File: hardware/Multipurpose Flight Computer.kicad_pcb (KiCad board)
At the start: 2 copper layers, 34.9 x 44.6 mm, 79 parts, among them J1 Screw_Terminal_01x02, J2 Conn_01x03, J3 Conn_01x03, SW1 TS-1088-AR02016, SW2 TS-1088-AR02016, U1 BQ25883RGER, U2 ICM-45686, U3 STM32F722RETx, U4 BMP580, U5 TPS63070RNMR, U6 LMR51430, X1 X322525MOB4SI, X2 Q13FC1350000400

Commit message: Updating KiCad
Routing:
- net GND: track 93.6 -> 98.2 mm
- net /BTST: vias 3 -> 2
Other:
- board size 34.9 x 44.6 mm -> 35.4 x 44.6 mm
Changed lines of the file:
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@@
 		(tags "resistor")
 		(property "Reference" "R15"
-			(at 2.59 0.15 0)
+			(at 0.015178 2.9 0)
 			(layer "F.SilkS")
 			(effects
@@
 		(tags "resistor")
 		(property "Reference" "R14"
-			(at -2.56 -0.05 0)
+			(at 0.064822 -2.6 0)
 			(layer "F.SilkS")
 			(effects
@@
 	)
 	(gr_rect
-		(start 125 120.4)
-		(end 159.95 165)
+		(start 124.95 120.75)
+		(end 160.35 165.35)
 		(stroke
 			(width 0.2)
@@
 	)
 	(segment
+		(start 148.965 159.7)
+		(end 148.965 160.575)
+		(width 0.3)
+		(layer "F.Cu")
+		(net 1)
+	)
+	(segment
 		(start 144.620927 147.55)
 		(end 144.125 147.55)
@@
 	)
 	(segment
+		(start 148.97 160.62)
+		(end 148.99 160.6)
+		(width 0.3)
+		(layer "F.Cu")
+		(net 1)
+	)
+	(segment
 		(start 151.300001 147.4)
 		(end 154.21 144.490001)
@@
 	)
 	(segment
+		(start 148.99 158.9)
+		(end 148.99 159.675)
+		(width 0.3)
+		(layer "F.Cu")
+		(net 1)
+	)
+	(segment
 		(start 148.174822 156.65)
 		(end 147.45 156.65)
@@
 	)
 	(segment
+		(start 148.97 161.45)
+		(end 148.97 160.62)
+		(width 0.3)
+		(layer "F.Cu")
+		(net 1)
+	)
+	(segment
 		(start 137.55 135.498)
 		(end 137.051 134.999)
@@
 	)
 	(segment
+		(start 148.965 158.875)
+		(end 148.99 158.9)
+		(width 0.3)
+		(layer "F.Cu")
+		(net 1)
+	)
+	(segment
 		(start 148.83 133.05)
 		(end 150.15 133.05)
@@
 	)
 	(segment
+		(start 148.99 159.675)
+		(end 148.965 159.7)
+		(width 0.3)
+		(layer "F.Cu")
+		(net 1)
+	)
+	(segment
 		(start 151.95 158.05)
 		(end 151.95 158.55)
@@
 	)
 	(segment
+		(start 148.965 158.05)
+		(end 148.965 158.875)
+		(width 0.3)
+		(layer "F.Cu")
+		(net 1)
+	)
+	(segment
 		(start 149.274822 156.65)
 		(end 148.174822 156.65)
@@
 	)
 	(segment
+		(start 148.97 162.27)
+		(end 149.2 162.5)
+		(width 0.3)
+		(layer "F.Cu")
+		(net 1)
+	)
+	(segment
 		(start 138.049 134.999)
 		(end 141.949 134.999)
@@
 	)
 	(segment
+		(start 148.965 160.575)
+		(end 148.99 160.6)
+		(width 0.3)
+		(layer "F.Cu")
+		(net 1)
+	)
+	(segment
 		(start 128.010124 149.66802)
 		(end 127.4382 150.239944)
@@
 	)
 	(segment
+		(start 148.97 161.45)
+		(end 148.97 162.27)
+		(width 0.3)
+		(layer "F.Cu")
+		(net 1)
+	)
+	(segment
 		(start 154.399822 158.6)
 		(end 156.070822 160.271)
@@
 	)
 	(via
-		(at 150.100001 147.05)
-		(size 0.6)
-		(drill 0.3)
-		(layers "F.Cu" "B.Cu")
-		(net 6)
-	)
-	(via
 		(at 149.950001 151.45)
 		(size 0.6)
@@
 		(layers "F.Cu" "B.Cu")
 		(hatch edge 0.5)
-		(connect_pads
+		(connect_pads yes
 			(clearance 0.5)
 		)
@@
 		(polygon
 			(pts
-				(xy 125.9 121.1) (xy 159.15 121.2) (xy 159.45 164.05) (xy 125.75 164.2)
+				(xy 121.95 117.9) (xy 166.05 117.15) (xy 167.15 168.4) (xy 121.25 167.35)
 			)
 		)

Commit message: Finishing Touches
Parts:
- added H1: MountingHole, MountingHole:MountingHole_2.2mm_M2_DIN965_Pad_TopBottom, F.Cu at (156.7, 124.8)
- moved C28 31.2 mm to (130.1, 137.5), turned to 90 degrees
- moved C19 29.1 mm to (128.3, 138.2), turned to 180 degrees
- moved C20 25.7 mm to (127.3, 139.9)
- moved C24 23.1 mm to (133.8, 140.4), turned to 45 degrees
- moved C23 22.1 mm to (137.4, 140.7), turned to -45 degrees
- moved C30 18.4 mm to (133.3, 156.0), turned to 45 degrees
- moved C26 17.7 mm to (131.8, 156.1), turned to -135 degrees
- moved C25 11.6 mm to (141.3, 151.7), turned to -90 degrees
- moved C31 11.0 mm to (142.2, 152.0), turned to -90 degrees
- moved R7 1.25 mm to (142.4, 148.6)
- moved R11 0.53 mm to (143.8, 151.8)
- moved C29 0.38 mm to (135.5, 139.8), turned to 0 degrees
- moved R10 0.34 mm to (143.7, 150.9)
- moved R9 0.27 mm to (143.5, 150.1)
- moved D1 0.18 mm to (144.3, 148.6)
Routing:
- net +3.3V: track 124.5 -> 128.1 mm, vias 9 -> 8
- net /SD_CMD: track 16.1 -> 16.7 mm
- net GND: track 98.2 -> 97.9 mm, vias 23 -> 30
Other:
- board size 35.4 x 44.6 mm -> 35.6 x 44.6 mm

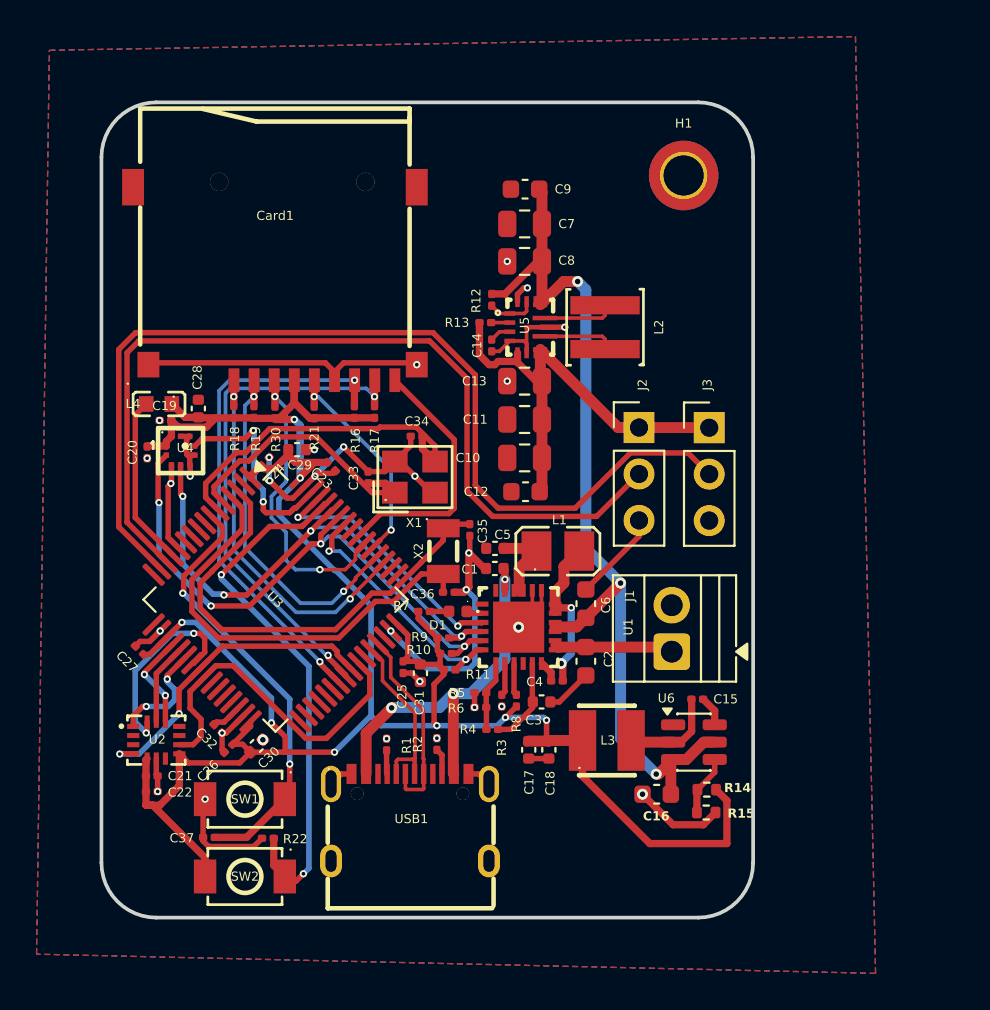
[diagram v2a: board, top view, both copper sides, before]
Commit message: 4-layer upgrade
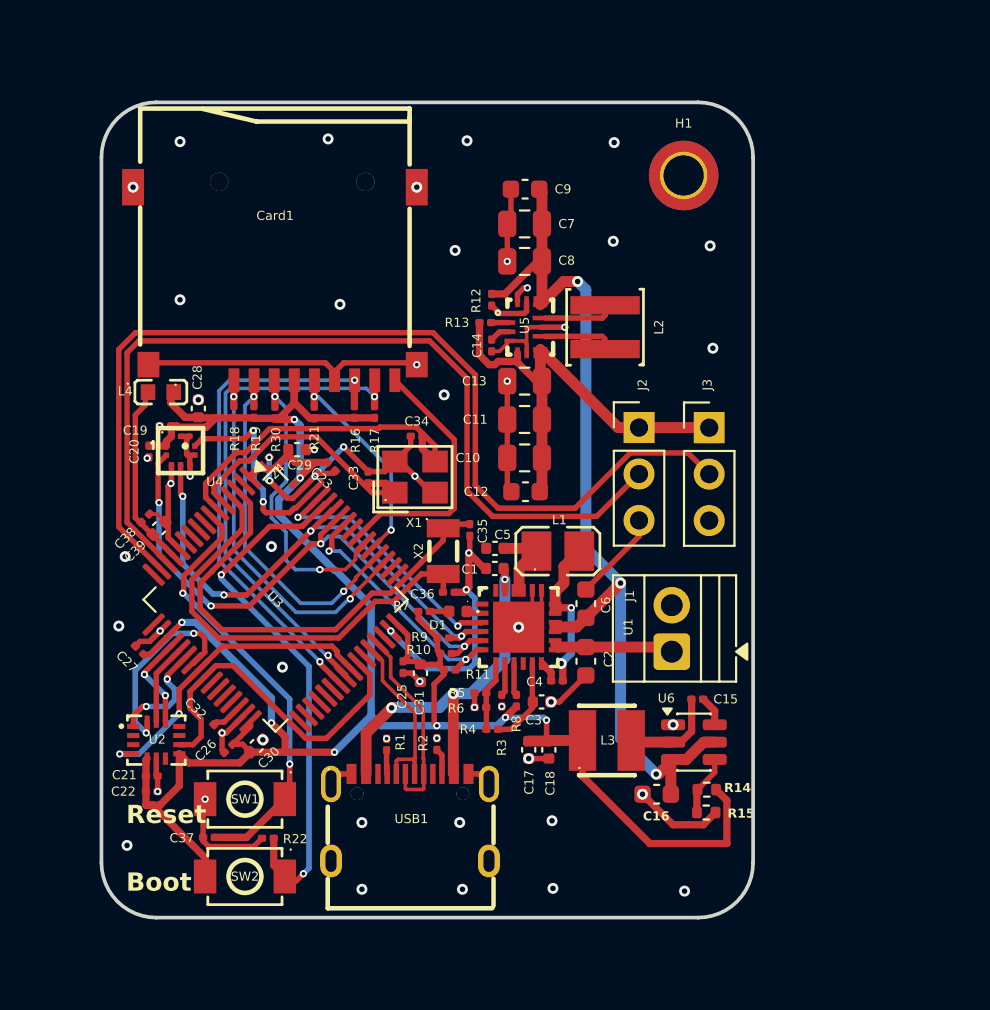
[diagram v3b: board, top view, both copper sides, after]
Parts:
- added C38: 100nF, Capacitor_SMD:C_0201_0603Metric, F.Cu at (127.2, 143.5)
- added C39: 1uF, Capacitor_SMD:C_0402_1005Metric, F.Cu at (128.0, 144.1)
- moved L4 0.66 mm to (128.1, 136.6)
- moved C19 0.30 mm to (128.3, 138.4)
- moved C20 0.11 mm to (127.4, 139.8)
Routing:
- net GND: track 97.9 -> 109.1 mm, vias 30 -> 59
- net Net-(U3-VDDA): track 9.39 -> 10.1 mm
- added copper zone on In1.Cu, net GND
- added copper zone on In2.Cu, net GND
- removed copper zone on B.Cu, net GND
- removed copper zone on F.Cu, net GND
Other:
- copper layers 2 -> 4
- board text added: "Boot"
- board text added: "Reset"

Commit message: fixing drc
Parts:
- moved R4 0.75 mm to (146.2, 155.8)
- moved C38 0.18 mm to (127.3, 143.4)
- moved C39 0.11 mm to (128.1, 144.0)
- moved R3 0.08 mm to (146.7, 153.4)
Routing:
- net +3.3V: track 128.3 -> 129.4 mm
- net Net-(U1-TS): track 3.82 -> 4.58 mm
- net GND: vias 59 -> 60

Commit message: minor edits
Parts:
- moved H1 1.31 mm to (155.7, 125.6)
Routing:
- net +3.3V: track 129.4 -> 128.8 mm
- net GND: vias 60 -> 65
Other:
- board size 35.6 x 44.6 mm -> 35 x 44.3 mm
- board text added: "MFC-1 Alex Miller"

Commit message: Finalized Board Design
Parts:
- added U7: TPD4EUSB30, Package_SON:USON-10_2.5x1.0mm_P0.5mm, F.Cu at (141.3, 154.3)
- moved C31 0.54 mm to (142.3, 151.4)
- moved R2 0.31 mm to (143.4, 155.9)
- moved R1 0.30 mm to (140.2, 156.1)
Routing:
- net +3.3V: track 128.8 -> 135.2 mm
- net GND: track 109.1 -> 104.4 mm, vias 65 -> 67
- net VBUS: track 21.5 -> 23.0 mm
- net /USB_DN: track 10.3 -> 11.1 mm, vias 0 -> 2
- net /USB_DP: track 10.8 -> 11.2 mm, vias 0 -> 2
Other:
- board text added: "+ -"
- board text added: "5V DAT GND"

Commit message: Bug Fixes
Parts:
- removed C20: 100nF, Capacitor_SMD:C_0201_0603Metric
- removed J1: Screw_Terminal_01x02, TerminalBlock:TerminalBlock_Xinya_XY308-2.54-2P_1x02_P2.54mm_Horizontal
- removed X2: Q13FC1350000400, easyeda2kicad:FC-135R_L3.2-W1.5
- added J4: Conn_01x02_Pin, easyeda2kicad:CONN-TH_XT30PW-M, F.Cu at (150.9, 128.1)
- added R20: 10K, Resistor_SMD:R_0201_0603Metric, F.Cu at (126.8, 151.8)
- added R23: 4.7k, Resistor_SMD:R_0201_0603Metric, F.Cu at (142.0, 140.8)
- C35: value 6.8pF -> 100nF
- C36: value 6.8pF -> 22uF; footprint Capacitor_SMD:C_0201_0603Metric -> Capacitor_SMD:C_0603_1608Metric
- C6: value 44uF -> 22uF
- C9: footprint Capacitor_SMD:C_0603_1608Metric -> Capacitor_SMD:C_0805_2012Metric
- R10, R9: value 10K -> 4.7k
- R3: value 3B3 -> 383; footprint Resistor_SMD:R_0201_0603Metric -> Resistor_SMD:R_0603_1608Metric
- R5: footprint Resistor_SMD:R_0201_0603Metric -> Resistor_SMD:R_0402_1005Metric
- moved H1 36.5 mm to (157.0, 162.1)
- moved C9 15.0 mm to (157.9, 136.7), turned to 90 degrees
- moved C34 13.8 mm to (128.7, 142.6)
- moved C19 13.4 mm to (141.2, 141.9), turned to 0 degrees
- moved X1 13.1 mm to (128.8, 140.5), turned to 180 degrees
- moved C7 12.2 mm to (155.8, 136.6), turned to 90 degrees
- moved U4 11.3 mm to (140.4, 140.6), turned to 180 degrees
- moved C35 10.6 mm to (136.0, 138.6), turned to 180 degrees
- moved R15 9.52 mm to (158.1, 150.1)
- moved R14 9.37 mm to (158.1, 149.0)
- moved C8 9.27 mm to (153.8, 136.6), turned to 90 degrees
- moved C36 8.65 mm to (151.7, 151.2), turned to -90 degrees
- moved C33 8.47 mm to (131.1, 139.8)
- moved C16 6.13 mm to (157.7, 153.0), turned to -90 degrees
- moved U6 5.68 mm to (155.4, 150.4), turned to 90 degrees
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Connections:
- C35 pad 1: /LSE_IN -> GND
- C35 pad 2: GND -> +3.3V
- C36 pad 1: /LSE_OUT -> VSYS
- U3 pad 3: /LSE_IN -> unconnected-(U3-PC14-Pad3)
- U3 pad 4: /LSE_OUT -> unconnected-(U3-PC15-Pad4)
- U4 pad 6: GND -> Net-(U4-CSB)
- U7 pad 10: unconnected-(U7-NC-Pad10) -> /USB_DP
- U7 pad 9: unconnected-(U7-NC-Pad9) -> /USB_DN
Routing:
- net BAT+: track 6.49 -> 37.8 mm, vias 0 -> 1
- net /LSE_IN: track 25.9 -> 0.00 mm
- net /LSE_OUT: track 24.5 -> 0.00 mm
- net GND: track 104.4 -> 125.2 mm, vias 67 -> 58
- net /SERVO2: track 54.9 -> 34.2 mm
- net /SERVO1: track 49.2 -> 29.2 mm
- net /HSE_OUT: track 18.5 -> 4.61 mm
- net +3.3V: track 135.2 -> 147.7 mm, vias 8 -> 9
- net /HSE_IN: track 15.1 -> 4.17 mm
- net /SD_DAT0: track 27.8 -> 37.2 mm
- net +5V: track 26.4 -> 18.5 mm
- net /BMP_INT: track 11.4 -> 3.80 mm
- net Net-(U4-CSB): track 0.00 -> 6.67 mm, vias 0 -> 2
- net /I2C_SDA: track 29.0 -> 23.5 mm, vias 4 -> 2
- net /I2C_SCL: track 31.5 -> 26.0 mm, vias 4 -> 2
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- added copper zone on B.Cu, net +5V
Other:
- board text added: "Alex M. MFC-1"
- board text added: "MFC-1"
- board text removed: "MFC-1 Alex Miller"

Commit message: Added software
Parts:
- moved C22 1.12 mm to (127.1, 159.5)
- moved C31 1.12 mm to (141.9, 152.5)
- moved C36 1.12 mm to (151.2, 152.2)
- moved C7 1.12 mm to (155.4, 137.7)
- moved C8 1.12 mm to (153.4, 137.7)
- moved L4 1.12 mm to (127.9, 139.0)
- moved R11 1.12 mm to (143.7, 152.2)
- moved R15 1.12 mm to (157.7, 151.1)
- moved R3 1.12 mm to (145.4, 156.2)
- moved R6 1.12 mm to (145.1, 155.0)
- moved R9 1.12 mm to (141.7, 149.5)
- moved U1 1.12 mm to (147.2, 150.5)
- moved U2 1.12 mm to (127.4, 156.7)
- moved R2 1.12 mm to (143.0, 157.0)
- moved C1 1.12 mm to (145.9, 147.3)
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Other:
- board text added: "Alex M. MFC-2"
- board text removed: "Alex M. MFC-1"
- board text removed: "MFC-1"
